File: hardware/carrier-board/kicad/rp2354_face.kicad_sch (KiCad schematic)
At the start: 0 parts

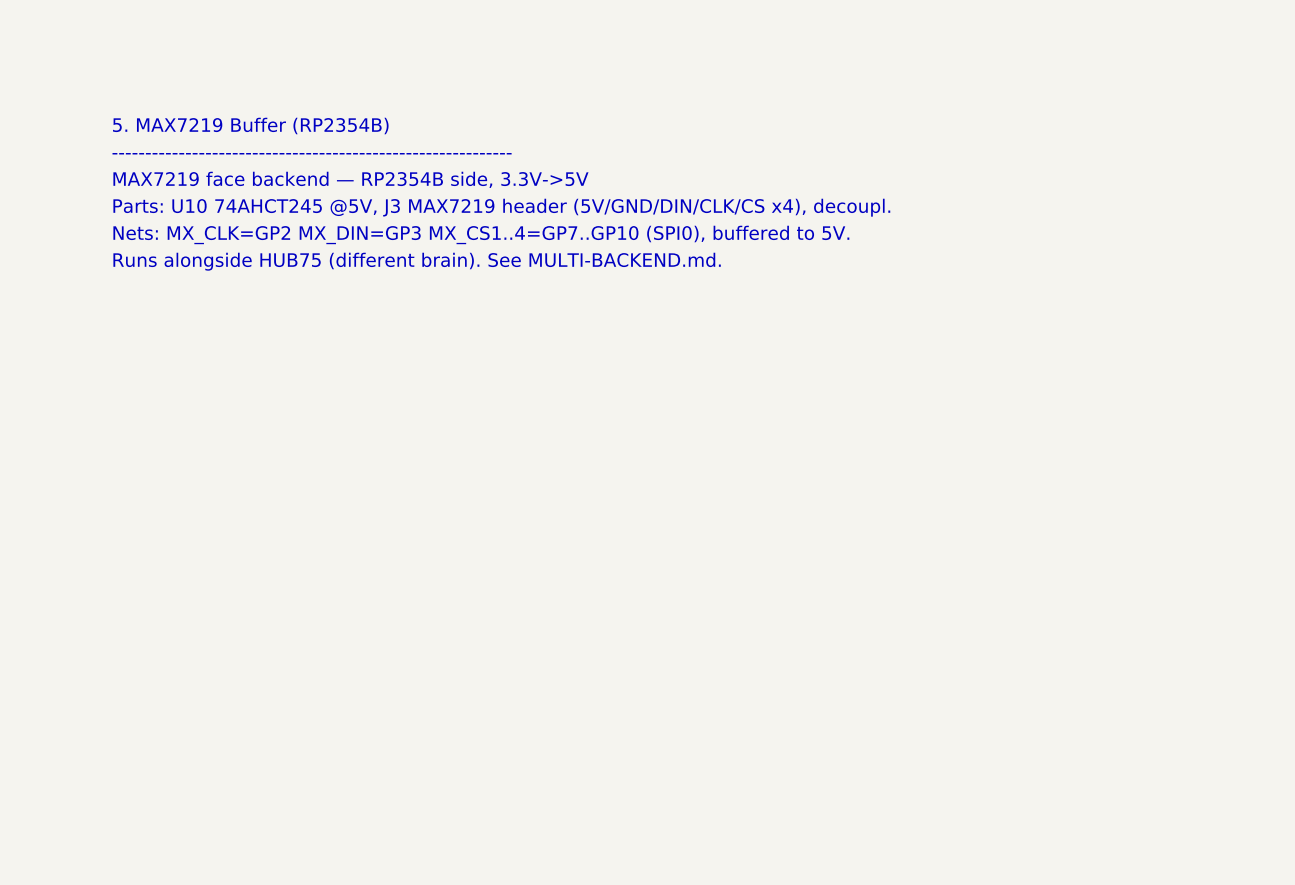
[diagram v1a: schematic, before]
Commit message: Carrier KiCad: populate all 11 schematic sheets
Replace populate_face_buffer.py with populate_sheets.py: one generator that
emits all 11 populated sub-sheets reusing the KiCad-9 format proven by the
face_buffer proof. Shared symbol library + generic box-symbol builder; condensed
CM5 (2x DF40-100) and RP2354B (QFN-80) symbols showing only used pins.

Connectivity by net labels (global for rails + cross-sheet nets: GPIOxx HUB75,
MX_*, LED*_DAT, SRV*, BTN*, *_USB_*; local within-sheet). Sheets: power
(protection + rails + AP2112 +3V3_RP), cm5 (HUB75 out + fan MOSFETs + RP ctrl),
face_buffer, rp2354_io (RP2354B + xtal + SW1/J12 + ESD + SWD), rp2354_face
(U10->J3), leds (U11 quad ->J4a-d), sensors_i2c (pull-ups+J5+STEMMA),
servos (J20-27 + rail), gpio_buttons (J6), usb (USB2514B hub + uplink),
cameras_display (CSI FFC + HDMI).

Verified: all sheets paren-balanced, every used lib_id defined, all instance
paths match sheet UUIDs, root<->sub-sheet UUID linkage intact. generate_skeleton.py
now lists all sheets POPULATED (writes only root+project). Not yet opened in
KiCad here -- expect ERC warnings (PWR_FLAG, unconnected pins) to clean.
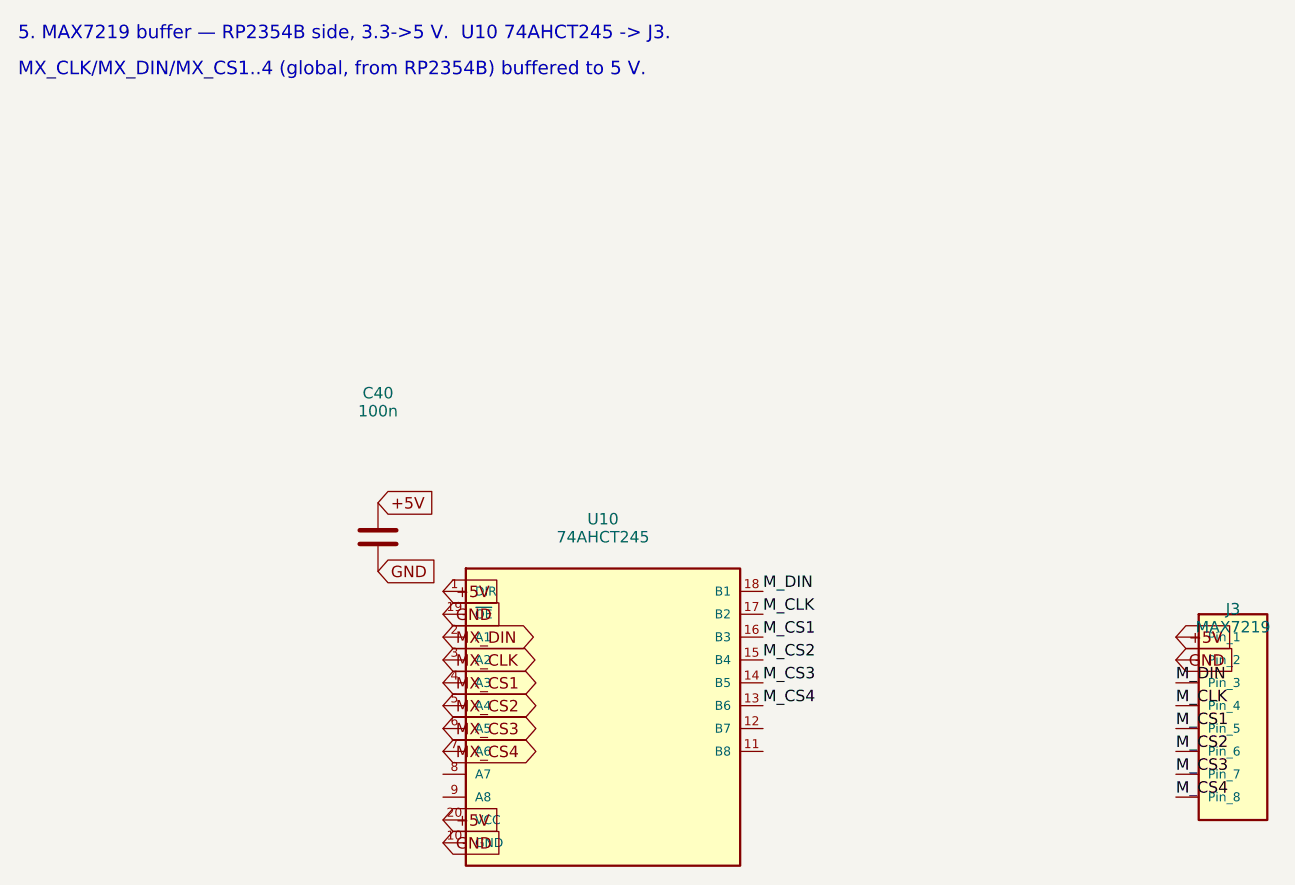
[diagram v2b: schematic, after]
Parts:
- added C40: 100n, symbol Device:C
- added J3: MAX7219, symbol Connector_Generic:Conn_01x08
- added U10: 74AHCT245, symbol 74xx:74AHCT245
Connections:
- new net +5V: C40.1, J3.1 (Pin_1), U10.1 (DIR), U10.20 (VCC)
- new net GND: C40.2, J3.2 (Pin_2), U10.10 (GND), U10.19 (~{OE})
- new net MX_CLK: U10.3 (A2)
- new net MX_CS1: U10.4 (A3)
- new net MX_CS2: U10.5 (A4)
- new net MX_CS3: U10.6 (A5)
- new net MX_CS4: U10.7 (A6)
- new net MX_DIN: U10.2 (A1)
- new net M_CLK: J3.4 (Pin_4), U10.17 (B2)
- new net M_CS1: J3.5 (Pin_5), U10.16 (B3)
- new net M_CS2: J3.6 (Pin_6), U10.15 (B4)
- new net M_CS3: J3.7 (Pin_7), U10.14 (B5)
- new net M_CS4: J3.8 (Pin_8), U10.13 (B6)
- new net M_DIN: J3.3 (Pin_3), U10.18 (B1)
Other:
- note added: "5. MAX7219 buffer — RP2354B side, 3.3->5 V. U10 74AHCT245 -> J3."
- note added: "MX_CLK/MX_DIN/MX_CS1..4 (global, from RP2354B) buffered to 5 V."
- note removed: "------------------------------------------------------------"
- note removed: "5. MAX7219 Buffer (RP2354B)"
- note removed: "MAX7219 face backend — RP2354B side, 3.3V->5V"
- note removed: "Nets: MX_CLK=GP2 MX_DIN=GP3 MX_CS1..4=GP7..GP10 (SPI0), buffered to 5V."
- note removed: "Parts: U10 74AHCT245 @5V, J3 MAX7219 header (5V/GND/DIN/CLK/CS x4), decoupl."
- note removed: "Runs alongside HUB75 (different brain). See MULTI-BACKEND.md."
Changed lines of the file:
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@@
 (kicad_sch
-  (version 20230121)
-  (generator protohud_skeleton)
+  (version 20250114)
+  (generator "protohud_populate")
+  (generator_version "9.0")
   (paper "A3")
   (title_block
@@
     (company "ProtoHUD")
   )
-  (text "5. MAX7219 Buffer (RP2354B)" (at 25.4 25.40 0) (effects (font (size 1.5 1.5)) (justify left bottom)))
-  (text "------------------------------------------------------------" (at 25.4 28.40 0) (effects (font (size 1.5 1.5)) (justify left bottom)))
-  (text "MAX7219 face backend — RP2354B side, 3.3V->5V" (at 25.4 31.40 0) (effects (font (size 1.5 1.5)) (justify left bottom)))
-  (text "Parts: U10 74AHCT245 @5V, J3 MAX7219 header (5V/GND/DIN/CLK/CS x4), decoupl." (at 25.4 34.40 0) (effects (font (size 1.5 1.5)) (justify left bottom)))
-  (text "Nets: MX_CLK=GP2 MX_DIN=GP3 MX_CS1..4=GP7..GP10 (SPI0), buffered to 5V." (at 25.4 37.40 0) (effects (font (size 1.5 1.5)) (justify left bottom)))
-  (text "Runs alongside HUB75 (different brain). See MULTI-BACKEND.md." (at 25.4 40.40 0) (effects (font (size 1.5 1.5)) (justify left bottom)))
+  (text "5. MAX7219 buffer — RP2354B side, 3.3->5 V.  U10 74AHCT245 -> J3." (at 15 15.0 0) (effects (font (size 1.5 1.5)) (justify left bottom)))
+  (text "MX_CLK/MX_DIN/MX_CS1..4 (global, from RP2354B) buffered to 5 V." (at 15 19.0 0) (effects (font (size 1.5 1.5)) (justify left bottom)))
+  (symbol
+    (lib_id "74xx:74AHCT245")
+    (at 80.00 90.00 0)
+    (unit 1)
+    (exclude_from_sim no) (in_bom yes) (on_board yes) (dnp no)
+    (property "Reference" "U10" (at 80.00 68.00 0) (effects (font (size 1.27 1.27))))
+    (property "Value" "74AHCT245" (at 80.00 70.00 0) (effects (font (size 1.27 1.27))))
+    (property "Footprint" "" (at 80.00 90.00 0) (effects (font (size 1.27 1.27)) (hide yes)))
+    (property "Datasheet" "" (at 80.00 90.00 0) (effects (font (size 1.27 1.27)) (hide yes)))
+    (pin "1")
+    (pin "19")
+    (pin "2")
+    (pin "3")
+    (pin "4")
+    (pin "5")
+    (pin "6")
+    (pin "7")
+    (pin "8")
+    (pin "9")
+    (pin "20")
+    (pin "10")
+    (pin "18")
+    (pin "17")
+    (pin "16")
+    (pin "15")
+    (pin "14")
+    (pin "13")
+    (pin "12")
+    (pin "11")
+    (instances
+      (project "ProtoHUD-Carrier"
+        (path "/a1b2c3d4-0002-4aaa-9bbb-000000000005"
+          (reference "U10") (unit 1))))
+  )
+  (symbol
+    (lib_id "Connector_Generic:Conn_01x08")
+    (at 150.00 90.00 0)
+    (unit 1)
+    (exclude_from_sim no) (in_bom yes) (on_board yes) (dnp no)
+    (property "Reference" "J3" (at 150.00 78.00 0) (effects (font (size 1.27 1.27))))
+    (property "Value" "MAX7219" (at 150.00 80.00 0) (effects (font (size 1.27 1.27))))
+    (property "Footprint" "" (at 150.00 90.00 0) (effects (font (size 1.27 1.27)) (hide yes)))
+    (property "Datasheet" "" (at 150.00 90.00 0) (effects (font (size 1.27 1.27)) (hide yes)))
+    (pin "1")
+    (pin "2")
+    (pin "3")
+    (pin "4")
+    (pin "5")
+    (pin "6")
+    (pin "7")
+    (pin "8")
+    (instances
+      (project "ProtoHUD-Carrier"
+        (path "/a1b2c3d4-0002-4aaa-9bbb-000000000005"
+          (reference "J3") (unit 1))))
+  )
+  (symbol
+    (lib_id "Device:C")
+    (at 55.00 70.00 0)
+    (unit 1)
+    (exclude_from_sim no) (in_bom yes) (on_board yes) (dnp no)
+    (property "Reference" "C40" (at 55.00 54.00 0) (effects (font (size 1.27 1.27))))
+    (property "Value" "100n" (at 55.00 56.00 0) (effects (font (size 1.27 1.27))))
+    (property "Footprint" "" (at 55.00 70.00 0) (effects (font (size 1.27 1.27)) (hide yes)))
+    (property "Datasheet" "" (at 55.00 70.00 0) (effects (font (size 1.27 1.27)) (hide yes)))
+    (pin "1")
+    (pin "2")
+    (instances
+      (project "ProtoHUD-Carrier"
+        (path "/a1b2c3d4-0002-4aaa-9bbb-000000000005"
+          (reference "C40") (unit 1))))
+  )
+  (global_label "+5V" (shape input) (at 62.22 76.03 180) (effects (font (size 1.27 1.27)) (justify left)))
+  (global_label "GND" (shape input) (at 62.22 78.57 180) (effects (font (size 1.27 1.27)) (justify left)))
+  (global_label "+5V" (shape input) (at 62.22 101.43 180) (effects (font (size 1.27 1.27)) (justify left)))
+  (global_label "GND" (shape input) (at 62.22 103.97 180) (effects (font (size 1.27 1.27)) (justify left)))
+  (global_label "MX_DIN" (shape bidirectional) (at 62.22 81.11 180) (effects (font (size 1.27 1.27)) (justify left)))
+  (label "M_DIN" (at 97.78 76.03 0) (effects (font (size 1.27 1.27)) (justify left bottom)))
+  (global_label "MX_CLK" (shape bidirectional) (at 62.22 83.65 180) (effects (font (size 1.27 1.27)) (justify left)))
+  (label "M_CLK" (at 97.78 78.57 0) (effects (font (size 1.27 1.27)) (justify left bottom)))
+  (global_label "MX_CS1" (shape bidirectional) (at 62.22 86.19 180) (effects (font (size 1.27 1.27)) (justify left)))
+  (label "M_CS1" (at 97.78 81.11 0) (effects (font (size 1.27 1.27)) (justify left bottom)))
+  (global_label "MX_CS2" (shape bidirectional) (at 62.22 88.73 180) (effects (font (size 1.27 1.27)) (justify left)))
+  (label "M_CS2" (at 97.78 83.65 0) (effects (font (size 1.27 1.27)) (justify left bottom)))
+  (global_label "MX_CS3" (shape bidirectional) (at 62.22 91.27 180) (effects (font (size 1.27 1.27)) (justify left)))
+  (label "M_CS3" (at 97.78 86.19 0) (effects (font (size 1.27 1.27)) (justify left bottom)))
+  (global_label "MX_CS4" (shape bidirectional) (at 62.22 93.81 180) (effects (font (size 1.27 1.27)) (justify left)))
+  (label "M_CS4" (at 97.78 88.73 0) (effects (font (size 1.27 1.27)) (justify left bottom)))
+  (global_label "+5V" (shape input) (at 143.65 81.11 180) (effects (font (size 1.27 1.27)) (justify left)))
+  (global_label "GND" (shape input) (at 143.65 83.65 180) (effects (font (size 1.27 1.27)) (justify left)))
+  (label "M_DIN" (at 143.65 86.19 180) (effects (font (size 1.27 1.27)) (justify left bottom)))
+  (label "M_CLK" (at 143.65 88.73 180) (effects (font (size 1.27 1.27)) (justify left bottom)))
+  (label "M_CS1" (at 143.65 91.27 180) (effects (font (size 1.27 1.27)) (justify left bottom)))
+  (label "M_CS2" (at 143.65 93.81 180) (effects (font (size 1.27 1.27)) (justify left bottom)))
+  (label "M_CS3" (at 143.65 96.35 180) (effects (font (size 1.27 1.27)) (justify left bottom)))
+  (label "M_CS4" (at 143.65 98.89 180) (effects (font (size 1.27 1.27)) (justify left bottom)))
+  (global_label "+5V" (shape input) (at 55.00 66.19 0) (effects (font (size 1.27 1.27)) (justify left)))
+  (global_label "GND" (shape input) (at 55.00 73.81 0) (effects (font (size 1.27 1.27)) (justify left)))
   (sheet_instances
     (path "/" (page "1"))
